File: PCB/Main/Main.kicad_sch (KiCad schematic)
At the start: 2 parts, among them J1 PICO LEFT, J2 PICO Right

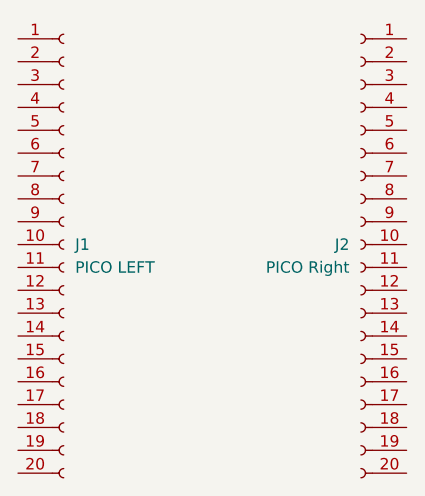
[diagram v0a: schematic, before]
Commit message: PCB editing
changes to footprints.
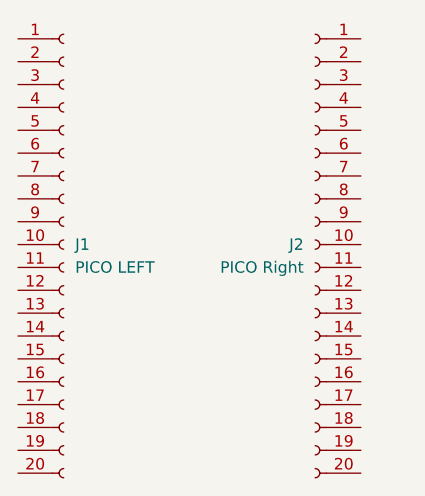
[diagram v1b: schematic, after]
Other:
- moved on the sheet: J2
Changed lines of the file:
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@@
 	(symbol
 		(lib_id "Connector:Conn_01x20_Socket")
-		(at 143.51 92.71 0)
+		(at 138.43 92.71 0)
 		(mirror y)
 		(unit 1)
@@
 		(dnp no)
 		(property "Reference" "J2"
-			(at 142.24 92.7099 0)
+			(at 137.16 92.7099 0)
 			(effects
 				(font
@@
 		)
 		(property "Value" "PICO Right"
-			(at 142.24 95.2499 0)
+			(at 137.16 95.2499 0)
 			(effects
 				(font
@@
 		)
 		(property "Footprint" "Connector_PinSocket_2.54mm:PinSocket_1x20_P2.54mm_Vertical"
-			(at 143.51 92.71 0)
+			(at 138.43 92.71 0)
 			(effects
 				(font
@@
 		)
 		(property "Datasheet" "~"
-			(at 143.51 92.71 0)
+			(at 138.43 92.71 0)
 			(effects
 				(font
@@
 		)
 		(property "Description" "Generic connector, single row, 01x20, script generated"
-			(at 143.51 92.71 0)
+			(at 138.43 92.71 0)
 			(effects
 				(font

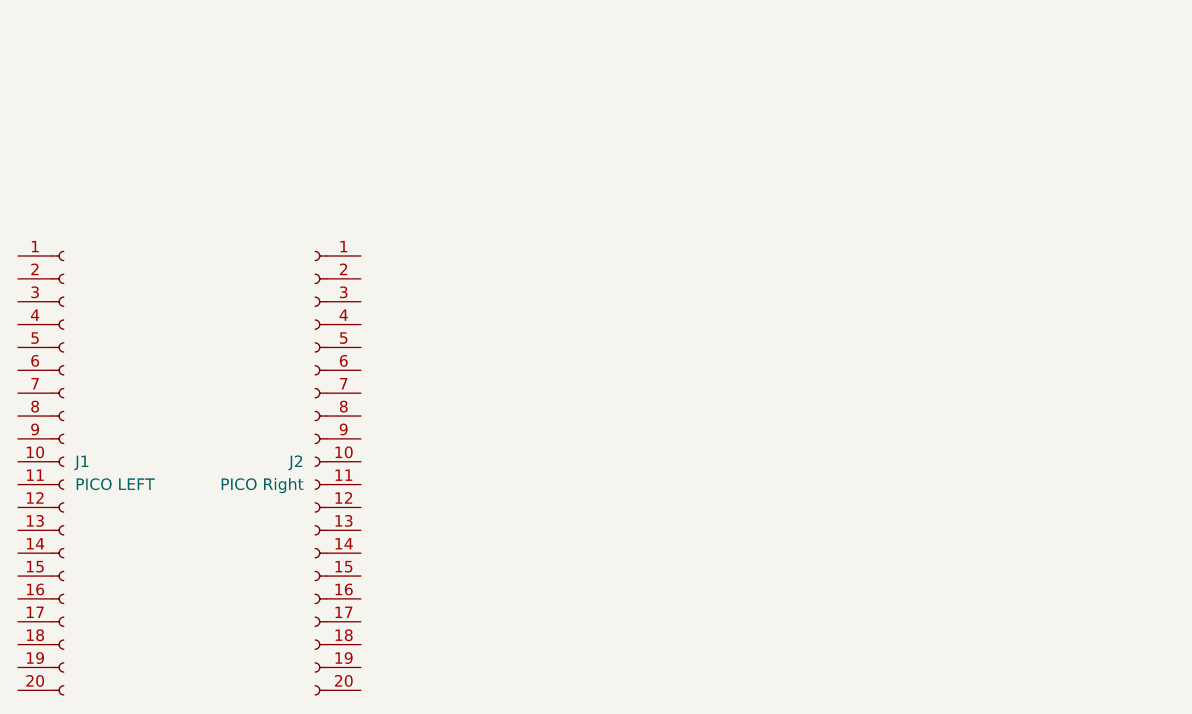
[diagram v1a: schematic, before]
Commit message: PLACED TB6612FNG Motor driver on schematic.
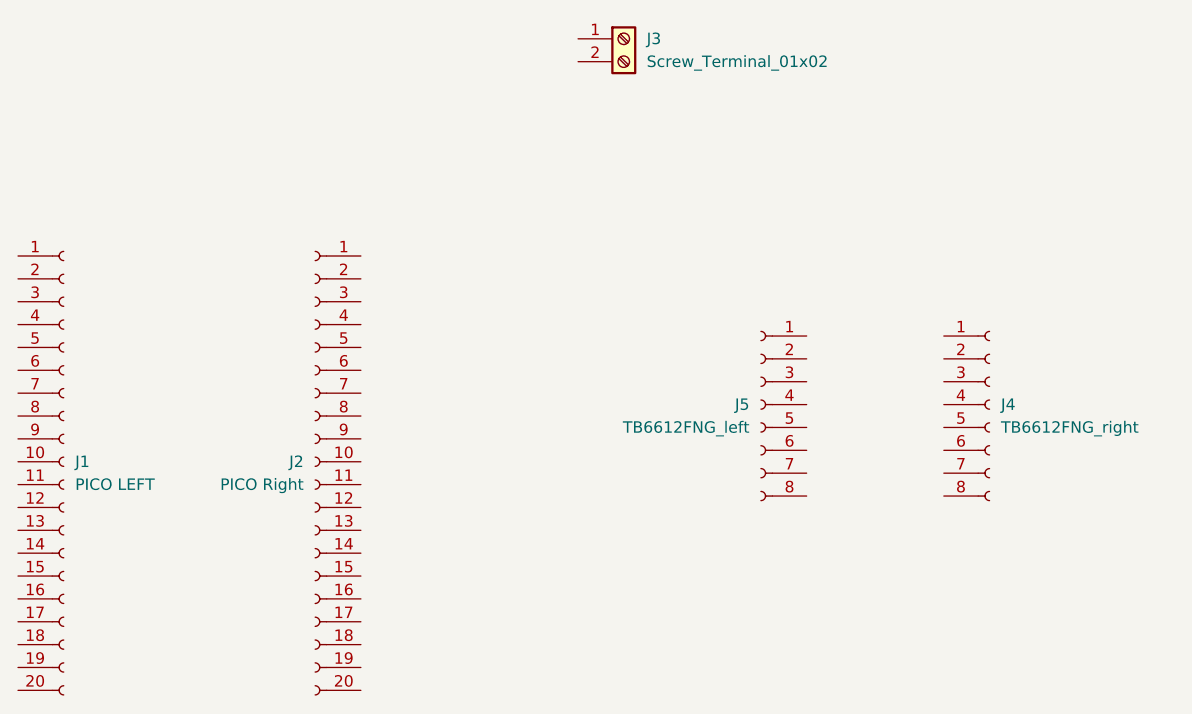
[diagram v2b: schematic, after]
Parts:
- added J3: Screw_Terminal_01x02, TerminalBlock_MetzConnect:TerminalBlock_MetzConnect_Type073_RT02602HBLU_1x02_P5.08mm_Horizontal, symbol Connector:Screw_Terminal_01x02
- added J4: TB6612FNG_right, Connector_PinSocket_2.54mm:PinSocket_1x08_P2.54mm_Vertical, symbol Connector:Conn_01x08_Socket
- added J5: TB6612FNG_left, Connector_PinSocket_2.54mm:PinSocket_1x08_P2.54mm_Vertical, symbol Connector:Conn_01x08_Socket
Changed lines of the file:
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@@
+		)
+	)
+	(symbol
+		(lib_id "Connector:Conn_01x08_Socket")
+		(at 187.96 86.36 0)
+		(mirror y)
+		(unit 1)
+		(exclude_from_sim no)
+		(in_bom yes)
+		(on_board yes)
+		(dnp no)
+		(property "Reference" "J5"
+			(at 186.69 86.3599 0)
+			(effects
+				(font
+					(size 1.27 1.27)
+				)
+				(justify left)
+			)
+		)
+		(property "Value" "TB6612FNG_left"
+			(at 186.69 88.8999 0)
+			(effects
+				(font
+					(size 1.27 1.27)
+				)
+				(justify left)
+			)
+		)
+		(property "Footprint" "Connector_PinSocket_2.54mm:PinSocket_1x08_P2.54mm_Vertical"
+			(at 187.96 86.36 0)
+			(effects
+				(font
+					(size 1.27 1.27)
+				)
+				(hide yes)
+			)
+		)
+		(property "Datasheet" "~"
+			(at 187.96 86.36 0)
+			(effects
+				(font
+					(size 1.27 1.27)
+				)
+				(hide yes)
+			)
+		)
+		(property "Description" "Generic connector, single row, 01x08, script generated"
+			(at 187.96 86.36 0)
+			(effects
+				(font
+					(size 1.27 1.27)
+				)
+				(hide yes)
+			)
+		)
+		(pin "1"
+		)
+		(pin "3"
+		)
+		(pin "6"
+		)
+		(pin "7"
+		)
+		(pin "2"
+		)
+		(pin "4"
+		)
+		(pin "8"
+		)
+		(pin "5"
+		)
+		(instances
+			(project "Main"
+				(path "/a194b5fc-75bd-402e-b15a-b617cc8492b3"
+					(reference "J5")
+					(unit 1)
+				)
+			)
+		)
+	)
+	(symbol
+		(lib_id "Connector:Conn_01x08_Socket")
+		(at 213.36 86.36 0)
+		(unit 1)
+		(exclude_from_sim no)
+		(in_bom yes)
+		(on_board yes)
+		(dnp no)
+		(fields_autoplaced yes)
+		(property "Reference" "J4"
+			(at 214.63 86.3599 0)
+			(effects
+				(font
+					(size 1.27 1.27)
+				)
+				(justify left)
+			)
+		)
+		(property "Value" "TB6612FNG_right"
+			(at 214.63 88.8999 0)
+			(effects
+				(font
+					(size 1.27 1.27)
+				)
+				(justify left)
+			)
+		)
+		(property "Footprint" "Connector_PinSocket_2.54mm:PinSocket_1x08_P2.54mm_Vertical"
+			(at 213.36 86.36 0)
+			(effects
+				(font
+					(size 1.27 1.27)
+				)
+				(hide yes)
+			)
+		)
+		(property "Datasheet" "~"
+			(at 213.36 86.36 0)
+			(effects
+				(font
+					(size 1.27 1.27)
+				)
+				(hide yes)
+			)
+		)
+		(property "Description" "Generic connector, single row, 01x08, script generated"
+			(at 213.36 86.36 0)
+			(effects
+				(font
+					(size 1.27 1.27)
+				)
+				(hide yes)
+			)
+		)
+		(pin "1"
+		)
+		(pin "3"
+		)
+		(pin "6"
+		)
+		(pin "7"
+		)
+		(pin "2"
+		)
+		(pin "4"
+		)
+		(pin "8"
+		)
+		(pin "5"
+		)
+		(instances
+			(project ""
+				(path "/a194b5fc-75bd-402e-b15a-b617cc8492b3"
+					(reference "J4")
+					(unit 1)
+				)
+			)
+		)
+	)
+	(symbol
+		(lib_id "Connector:Screw_Terminal_01x02")
+		(at 172.72 45.72 0)
+		(unit 1)
+		(exclude_from_sim no)
+		(in_bom yes)
+		(on_board yes)
+		(dnp no)
+		(fields_autoplaced yes)
+		(property "Reference" "J3"
+			(at 175.26 45.7199 0)
+			(effects
+				(font
+					(size 1.27 1.27)
+				)
+				(justify left)
+			)
+		)
+		(property "Value" "Screw_Terminal_01x02"
+			(at 175.26 48.2599 0)
+			(effects
+				(font
+					(size 1.27 1.27)
+				)
+				(justify left)
+			)
+		)
+		(property "Footprint" "TerminalBlock_MetzConnect:TerminalBlock_MetzConnect_Type073_RT02602HBLU_1x02_P5.08mm_Horizontal"
+			(at 172.72 45.72 0)
+			(effects
+				(font
+					(size 1.27 1.27)
+				)
+				(hide yes)
+			)
+		)
+		(property "Datasheet" "~"
+			(at 172.72 45.72 0)
+			(effects
+				(font
+					(size 1.27 1.27)
+				)
+				(hide yes)
+			)
+		)
+		(property "Description" "Generic screw terminal, single row, 01x02, script generated (kicad-library-utils/schlib/autogen/connector/)"
+			(at 172.72 45.72 0)
+			(effects
+				(font
+					(size 1.27 1.27)
+				)
+				(hide yes)
+			)
+		)
+		(pin "2"
+		)
+		(pin "1"
+		)
+		(instances
+			(project ""
+				(path "/a194b5fc-75bd-402e-b15a-b617cc8492b3"
+					(reference "J3")
+					(unit 1)
+				)
+			)
 		)
 	)
